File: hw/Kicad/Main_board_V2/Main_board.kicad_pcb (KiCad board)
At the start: 2 copper layers, 100 x 100 mm, 31 parts, among them J1 LIPO 2S, J10 DIST_FRONT, J11 SENSORES_LINEA, J12 DIST_DCHA, J2 MOT_IZQ, J3 TB6612FNG_A, J4 TB6612FNG_B, J5 DC-DC_5V, J6 HC-05, J7 MOT_DER, J8 DIST_IZQ, J9 CAMARA, SW1 SW_DPDT, SW2 SW_Push, SW3 SW_Push, U1 PCF8574

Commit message: Cambiado valor del diodo D4
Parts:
- D4: value 1N4001 -> 1N4148
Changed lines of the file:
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@@
-(kicad_pcb (version 4) (host pcbnew 4.0.7)
+(kicad_pcb (version 4) (host pcbnew 4.0.7-e2-6376~58~ubuntu16.04.1)
   (general
     (links 94)
-    (no_connects 2)
+    (no_connects 0)
     (area 99.899999 44.8 200.100001 150.100001)
     (thickness 1.6)
@@
       (effects (font (size 1 1) (thickness 0.15)))
     )
-    (fp_text value 1N4001 (at 5.08 2.41 180) (layer F.Fab)
-      (effects (font (size 1 1) (thickness 0.15)))
-    )
+    (fp_text value 1N4148 (at 5.08 2.41 180) (layer F.Fab)
+      (effects (font (size 1 1) (thickness 0.15)))
+    )

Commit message: PCBs silkscreen updated
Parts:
- removed the G*** at (150.0, 127.0)
- added G***: LOGO, Main_board:Logo Puma Pride, B.Cu at (150.0, 123.0)
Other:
- board text added: "Puma Pride Robotics Team"
- board text removed: "RESAJ"

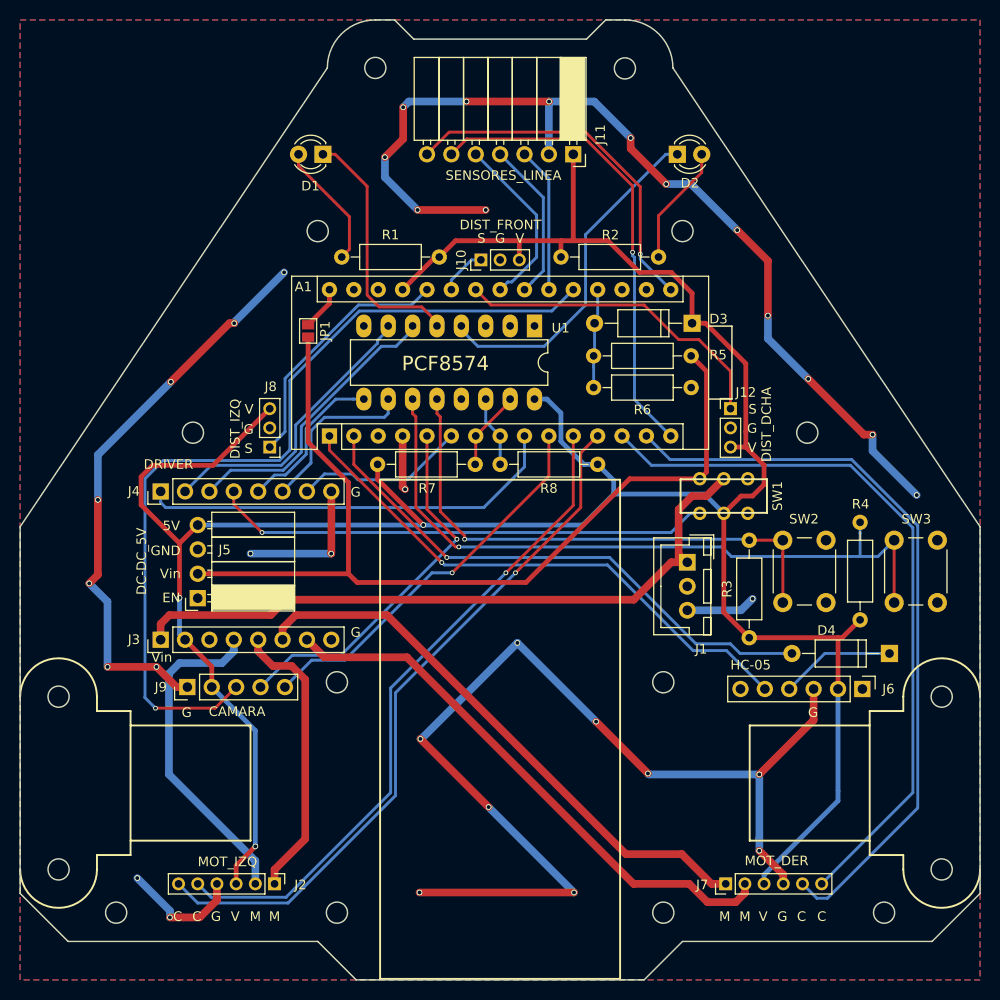
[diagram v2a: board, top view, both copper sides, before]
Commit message: PCBs adapted with Kicad libraries models
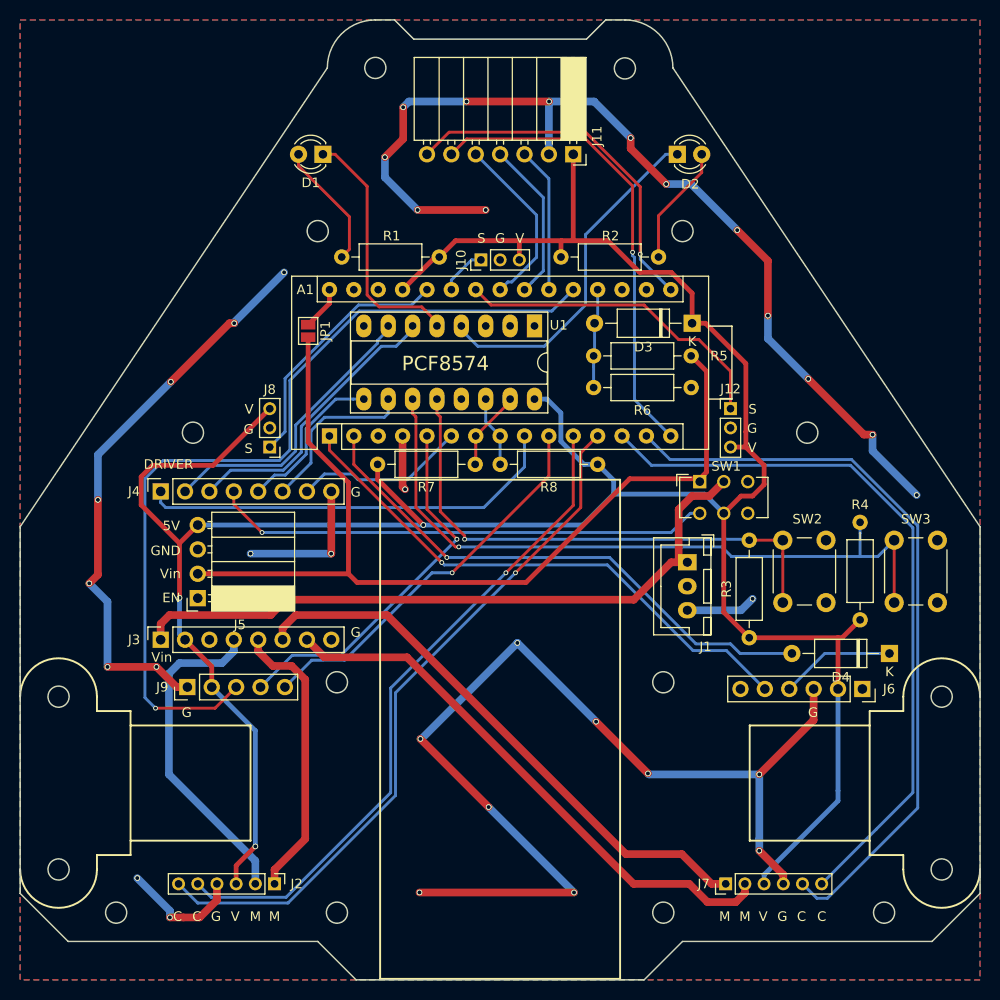
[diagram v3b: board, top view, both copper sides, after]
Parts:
- A1: footprint Modules:Arduino_Nano -> Main_board:Arduino_Nano
- D1, D2: footprint LEDs:LED_D3.0mm -> Main_board:LED_D3.0mm
- D3, D4: footprint Diodes_THT:D_A-405_P10.16mm_Horizontal -> Main_board:D_A-405_P10.16mm_Horizontal
- J1: footprint Connectors_JST:JST_XH_B03B-XH-A_03x2.50mm_Straight -> Main_board:JST_XH_B03B-XH-A_1x03_P2.50mm_Vertical
- J10, J12, J8: footprint Socket_Strips:Socket_Strip_Straight_1x03_Pitch2.00mm -> Main_board:PinHeader_1x03_P2.00mm_Vertical
- J11: footprint Socket_Strips:Socket_Strip_Angled_1x07_Pitch2.54mm -> Main_board:PinSocket_1x07_P2.54mm_Horizontal
- J2, J7: footprint Socket_Strips:Socket_Strip_Straight_1x06_Pitch2.00mm -> Main_board:PinHeader_1x06_P2.00mm_Vertical
- J3, J4: footprint Socket_Strips:Socket_Strip_Straight_1x08_Pitch2.54mm -> Main_board:PinSocket_1x08_P2.54mm_Vertical
- J5: footprint Socket_Strips:Socket_Strip_Angled_1x04_Pitch2.54mm -> Main_board:PinSocket_1x04_P2.54mm_Horizontal
- J6: footprint Socket_Strips:Socket_Strip_Straight_1x06_Pitch2.54mm -> Main_board:PinSocket_1x06_P2.54mm_Vertical
- J9: footprint Socket_Strips:Socket_Strip_Straight_1x05_Pitch2.54mm -> Main_board:PinHeader_1x05_P2.54mm_Vertical
- JP1: footprint Connectors:GS2 -> Main_board:SolderJumper-2_P1.3mm_Open_Pad1.0x1.5mm
- R1, R2, R3, R4, R5, R6, R7, R8: footprint Resistors_THT:R_Axial_DIN0207_L6.3mm_D2.5mm_P10.16mm_Horizontal -> Main_board:R_Axial_DIN0207_L6.3mm_D2.5mm_P10.16mm_Horizontal
- SW1: footprint Main_board:switch_DPDT -> Main_board:SW_CuK_JS202011CQN_DPDT_Straight
- SW2, SW3: footprint Buttons_Switches_THT:SW_PUSH_6mm -> Main_board:SW_PUSH_6mm
- U1: footprint Housings_DIP:DIP-16_W7.62mm_LongPads -> Main_board:DIP-16_W7.62mm_Socket_LongPads
- moved SW1 2.92 mm to (170.8, 98.1), turned to 0 degrees
- turned JP1 to 270 degrees
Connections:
- A1 pad 17: Net-(A1-Pad17) -> (no net)
- A1 pad 18: Net-(A1-Pad18) -> (no net)
- A1 pad 28: Net-(A1-Pad28) -> (no net)
- A1 pad 3: Net-(A1-Pad3) -> (no net)
- J1 pad 2: Net-(J1-Pad2) -> (no net)
- J5 pad 1: Net-(J5-Pad1) -> (no net)
- J6 pad 1: Net-(J6-Pad1) -> (no net)
- J6 pad 6: Net-(J6-Pad6) -> (no net)
- SW1 pad 1: Net-(SW1-Pad1) -> VDD
- SW1 pad 3: VDD -> (no net)
- SW1 pad 4: Net-(SW1-Pad4) -> STBY_MOT
- SW1 pad 6: STBY_MOT -> (no net)
- U1 pad 13: Net-(U1-Pad13) -> (no net)
